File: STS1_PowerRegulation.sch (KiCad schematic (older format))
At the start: 16 parts, among them U2 TPS61288

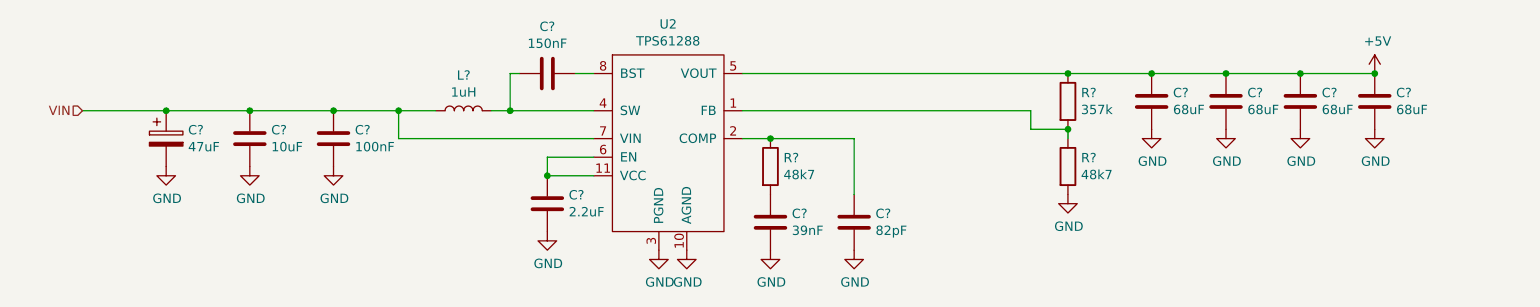
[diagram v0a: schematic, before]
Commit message: Select parts for dcdc converter
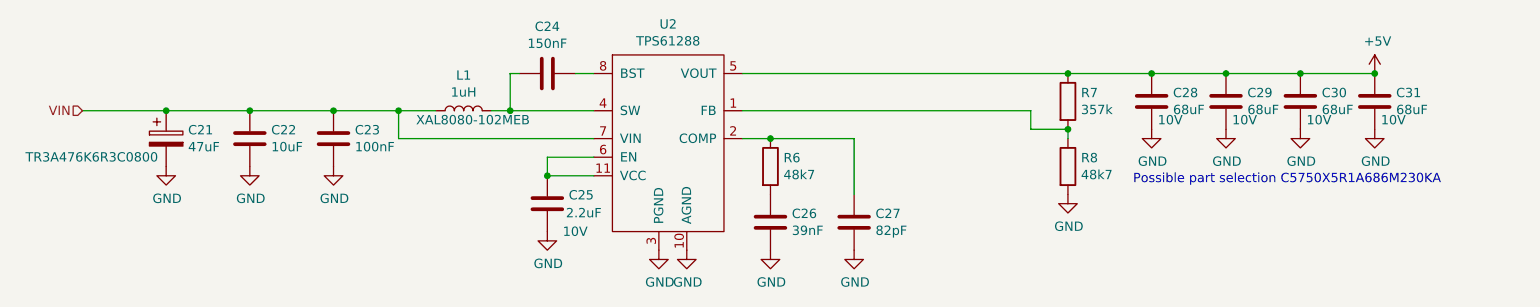
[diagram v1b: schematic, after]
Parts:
- C21: renamed from C?; footprint (none) -> Capacitor_Tantalum_SMD:CP_EIA-3216-18_Kemet-A; Part (none) -> TR3A476K6R3C0800
- C22: renamed from C?; footprint (none) -> Capacitor_SMD:C_1206_3216Metric
- C23, C24, C26, C27: renamed from C?; footprint (none) -> Capacitor_SMD:C_0603_1608Metric
- C25: renamed from C?; footprint (none) -> Capacitor_SMD:C_0603_1608Metric; Part (none) -> C1608X7R1A225K080AC; Voltage (none) -> 10V
- C28, C29, C30, C31: renamed from C?; footprint (none) -> Capacitor_SMD:C_2220_5650Metric; Part (none) -> C5750X5R1A686M230KA; Voltage (none) -> 10V
- L1: renamed from L?; footprint (none) -> STS1_DCDC:XAL8080; Part (none) -> XAL8080-102MEB
- R6, R7, R8: renamed from R?; footprint (none) -> Resistor_SMD:R_0603_1608Metric
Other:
- note added: "Possible part selection C5750X5R1A686M230KA"
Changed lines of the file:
@@
 $EndComp
 $Comp
-L Device:C C?
+L Device:C C25
 U 1 1 61712450
 P 4550 3300
-F 0 "C?" H 4665 3346 50  0000 L CNN
-F 1 "2.2uF" H 4665 3255 50  0000 L CNN
-F 2 "" H 4588 3150 50  0001 C CNN
+F 0 "C25" H 4665 3346 50  0000 L CNN
+F 1 "2.2uF" H 4650 3250 50  0000 L CNN
+F 2 "Capacitor_SMD:C_0603_1608Metric" H 4588 3150 50  0001 C CNN
 F 3 "~" H 4550 3300 50  0001 C CNN
+F 4 "10V" H 4700 3150 50  0000 C CNN "Voltage"
+F 5 "C1608X7R1A225K080AC " H 4550 3300 50  0001 C CNN "Part"
 	1    4550 3300
 	1    0    0    -1
 $EndComp
 $Comp
-L power:GND #PWR?
+L power:GND #PWR04
 U 1 1 61712809
 P 4550 3450
-F 0 "#PWR?" H 4550 3200 50  0001 C CNN
+F 0 "#PWR04" H 4550 3200 50  0001 C CNN
 F 1 "GND" H 4555 3277 50  0000 C CNN
 F 2 "" H 4550 3450 50  0001 C CNN
@@
 Connection ~ 4550 3150
 $Comp
-L Device:L L?
+L Device:L L1
 U 1 1 61712D19
 P 4100 2800
-F 0 "L?" V 4290 2800 50  0000 C CNN
+F 0 "L1" V 4290 2800 50  0000 C CNN
 F 1 "1uH" V 4199 2800 50  0000 C CNN
-F 2 "" H 4100 2800 50  0001 C CNN
+F 2 "STS1_DCDC:XAL8080" H 4100 2800 50  0001 C CNN
 F 3 "~" H 4100 2800 50  0001 C CNN
+F 4 "XAL8080-102MEB " V 4050 2750 50  0000 C CNN "Part"
 	1    4100 2800
 	0    -1   -1   0
@@
 	4250 2800 4350 2800
 $Comp
-L Device:C C?
+L Device:C C24
 U 1 1 617133FA
 P 4550 2600
-F 0 "C?" V 4298 2600 50  0000 C CNN
+F 0 "C24" V 4298 2600 50  0000 C CNN
 F 1 "150nF" V 4389 2600 50  0000 C CNN
-F 2 "" H 4588 2450 50  0001 C CNN
+F 2 "Capacitor_SMD:C_0603_1608Metric" H 4588 2450 50  0001 C CNN
 F 3 "~" H 4550 2600 50  0001 C CNN
 	1    4550 2600
@@
 	3750 2800 3950 2800
 $Comp
-L Device:C C?
+L Device:C C23
 U 1 1 61713BDE
 P 3400 2950
-F 0 "C?" H 3515 2996 50  0000 L CNN
+F 0 "C23" H 3515 2996 50  0000 L CNN
 F 1 "100nF" H 3515 2905 50  0000 L CNN
-F 2 "" H 3438 2800 50  0001 C CNN
+F 2 "Capacitor_SMD:C_0603_1608Metric" H 3438 2800 50  0001 C CNN
 F 3 "~" H 3400 2950 50  0001 C CNN
 	1    3400 2950
@@
 $EndComp
 $Comp
-L Device:C C?
+L Device:C C22
 U 1 1 61714238
 P 2950 2950
-F 0 "C?" H 3065 2996 50  0000 L CNN
+F 0 "C22" H 3065 2996 50  0000 L CNN
 F 1 "10uF" H 3065 2905 50  0000 L CNN
-F 2 "" H 2988 2800 50  0001 C CNN
+F 2 "Capacitor_SMD:C_1206_3216Metric" H 2988 2800 50  0001 C CNN
 F 3 "~" H 2950 2950 50  0001 C CNN
 	1    2950 2950
@@
 $EndComp
 $Comp
-L Device:CP C?
+L Device:CP C21
 U 1 1 61714747
 P 2500 2950
-F 0 "C?" H 2618 2996 50  0000 L CNN
+F 0 "C21" H 2618 2996 50  0000 L CNN
 F 1 "47uF" H 2618 2905 50  0000 L CNN
-F 2 "" H 2538 2800 50  0001 C CNN
+F 2 "Capacitor_Tantalum_SMD:CP_EIA-3216-18_Kemet-A" H 2538 2800 50  0001 C CNN
 F 3 "~" H 2500 2950 50  0001 C CNN
+F 4 "TR3A476K6R3C0800 " H 2100 2850 50  0000 C CNN "Part"
 	1    2500 2950
 	1    0    0    -1
 $EndComp
 $Comp
-L power:GND #PWR?
+L power:GND #PWR03
 U 1 1 61714EC5
 P 3400 3100
-F 0 "#PWR?" H 3400 2850 50  0001 C CNN
+F 0 "#PWR03" H 3400 2850 50  0001 C CNN
 F 1 "GND" H 3405 2927 50  0000 C CNN
 F 2 "" H 3400 3100 50  0001 C CNN
@@
 $EndComp
 $Comp
-L power:GND #PWR?
+L power:GND #PWR02
 U 1 1 617154C8
 P 2950 3100
-F 0 "#PWR?" H 2950 2850 50  0001 C CNN
+F 0 "#PWR02" H 2950 2850 50  0001 C CNN
 F 1 "GND" H 2955 2927 50  0000 C CNN
 F 2 "" H 2950 3100 50  0001 C CNN
@@
 $EndComp
 $Comp
-L power:GND #PWR?
+L power:GND #PWR01
 U 1 1 617158AD
 P 2500 3100
-F 0 "#PWR?" H 2500 2850 50  0001 C CNN
+F 0 "#PWR01" H 2500 2850 50  0001 C CNN
 F 1 "GND" H 2505 2927 50  0000 C CNN
 F 2 "" H 2500 3100 50  0001 C CNN
@@
 VIN
 $Comp
-L power:GND #PWR?
+L power:GND #PWR05
 U 1 1 617163D0
 P 5150 3550
-F 0 "#PWR?" H 5150 3300 50  0001 C CNN
+F 0 "#PWR05" H 5150 3300 50  0001 C CNN
 F 1 "GND" H 5155 3377 50  0000 C CNN
 F 2 "" H 5150 3550 50  0001 C CNN
@@
 $EndComp
 $Comp
-L power:GND #PWR?
+L power:GND #PWR06
 U 1 1 617168F0
 P 5300 3550
-F 0 "#PWR?" H 5300 3300 50  0001 C CNN
+F 0 "#PWR06" H 5300 3300 50  0001 C CNN
 F 1 "GND" H 5305 3377 50  0000 C CNN
 F 2 "" H 5300 3550 50  0001 C CNN
@@
 	5600 2600 7350 2600
 $Comp
-L Device:R R?
+L Device:R R7
 U 1 1 61717075
 P 7350 2750
-F 0 "R?" H 7420 2796 50  0000 L CNN
+F 0 "R7" H 7420 2796 50  0000 L CNN
 F 1 "357k" H 7420 2705 50  0000 L CNN
-F 2 "" V 7280 2750 50  0001 C CNN
+F 2 "Resistor_SMD:R_0603_1608Metric" V 7280 2750 50  0001 C CNN
 F 3 "~" H 7350 2750 50  0001 C CNN
 	1    7350 2750
@@
 $EndComp
 $Comp
-L Device:R R?
+L Device:R R8
 U 1 1 61717628
 P 7350 3100
-F 0 "R?" H 7420 3146 50  0000 L CNN
+F 0 "R8" H 7420 3146 50  0000 L CNN
 F 1 "48k7" H 7420 3055 50  0000 L CNN
-F 2 "" V 7280 3100 50  0001 C CNN
+F 2 "Resistor_SMD:R_0603_1608Metric" V 7280 3100 50  0001 C CNN
 F 3 "~" H 7350 3100 50  0001 C CNN
 	1    7350 3100
@@
 $EndComp
 $Comp
-L power:GND #PWR?
+L power:GND #PWR09
 U 1 1 61717E4B
 P 7350 3250
-F 0 "#PWR?" H 7350 3000 50  0001 C CNN
+F 0 "#PWR09" H 7350 3000 50  0001 C CNN
 F 1 "GND" H 7355 3077 50  0000 C CNN
 F 2 "" H 7350 3250 50  0001 C CNN
@@
 Connection ~ 7350 2900
 $Comp
-L Device:R R?
+L Device:R R6
 U 1 1 61718B8B
 P 5750 3100
-F 0 "R?" H 5820 3146 50  0000 L CNN
+F 0 "R6" H 5820 3146 50  0000 L CNN
 F 1 "48k7" H 5820 3055 50  0000 L CNN
-F 2 "" V 5680 3100 50  0001 C CNN
+F 2 "Resistor_SMD:R_0603_1608Metric" V 5680 3100 50  0001 C CNN
 F 3 "~" H 5750 3100 50  0001 C CNN
 	1    5750 3100
@@
 $EndComp
 $Comp
-L Device:C C?
+L Device:C C26
 U 1 1 617191CB
 P 5750 3400
-F 0 "C?" H 5865 3446 50  0000 L CNN
+F 0 "C26" H 5865 3446 50  0000 L CNN
 F 1 "39nF" H 5865 3355 50  0000 L CNN
-F 2 "" H 5788 3250 50  0001 C CNN
+F 2 "Capacitor_SMD:C_0603_1608Metric" H 5788 3250 50  0001 C CNN
 F 3 "~" H 5750 3400 50  0001 C CNN
 	1    5750 3400
@@
 $EndComp
 $Comp
-L power:GND #PWR?
+L power:GND #PWR07
 U 1 1 617197CA
 P 5750 3550
-F 0 "#PWR?" H 5750 3300 50  0001 C CNN
+F 0 "#PWR07" H 5750 3300 50  0001 C CNN
 F 1 "GND" H 5755 3377 50  0000 C CNN
 F 2 "" H 5750 3550 50  0001 C CNN
@@
 	5600 2950 5750 2950
 $Comp
-L Device:C C?
+L Device:C C27
 U 1 1 61719FDA
 P 6200 3400
-F 0 "C?" H 6315 3446 50  0000 L CNN
+F 0 "C27" H 6315 3446 50  0000 L CNN
 F 1 "82pF" H 6315 3355 50  0000 L CNN
-F 2 "" H 6238 3250 50  0001 C CNN
+F 2 "Capacitor_SMD:C_0603_1608Metric" H 6238 3250 50  0001 C CNN
 F 3 "~" H 6200 3400 50  0001 C CNN
 	1    6200 3400
@@
 $EndComp
 $Comp
-L power:GND #PWR?
+L power:GND #PWR08
 U 1 1 6171A582
 P 6200 3550
-F 0 "#PWR?" H 6200 3300 50  0001 C CNN
+F 0 "#PWR08" H 6200 3300 50  0001 C CNN
 F 1 "GND" H 6205 3377 50  0000 C CNN
 F 2 "" H 6200 3550 50  0001 C CNN
@@
 Connection ~ 5750 2950
 $Comp
-L Device:C C?
+L Device:C C28
 U 1 1 6171AF96
 P 7800 2750
-F 0 "C?" H 7915 2796 50  0000 L CNN
+F 0 "C28" H 7915 2796 50  0000 L CNN
 F 1 "68uF" H 7915 2705 50  0000 L CNN
-F 2 "" H 7838 2600 50  0001 C CNN
+F 2 "Capacitor_SMD:C_2220_5650Metric" H 7838 2600 50  0001 C CNN
 F 3 "~" H 7800 2750 50  0001 C CNN
+F 4 "10V" H 7900 2650 50  0000 C CNN "Voltage"
+F 5 "C5750X5R1A686M230KA " H 7800 2750 50  0001 C CNN "Part"
 	1    7800 2750
 	1    0    0    -1
 $EndComp
 $Comp
-L Device:C C?
+L Device:C C29
 U 1 1 6171B43B
 P 8200 2750
-F 0 "C?" H 8315 2796 50  0000 L CNN
+F 0 "C29" H 8315 2796 50  0000 L CNN
 F 1 "68uF" H 8315 2705 50  0000 L CNN
-F 2 "" H 8238 2600 50  0001 C CNN
+F 2 "Capacitor_SMD:C_2220_5650Metric" H 8238 2600 50  0001 C CNN
 F 3 "~" H 8200 2750 50  0001 C CNN
+F 4 "10V" H 8300 2650 50  0000 C CNN "Voltage"
+F 5 "C5750X5R1A686M230KA " H 8200 2750 50  0001 C CNN "Part"
 	1    8200 2750
 	1    0    0    -1
 $EndComp
 $Comp
-L Device:C C?
+L Device:C C30
 U 1 1 6171B9A7
 P 8600 2750
-F 0 "C?" H 8715 2796 50  0000 L CNN
+F 0 "C30" H 8715 2796 50  0000 L CNN
 F 1 "68uF" H 8715 2705 50  0000 L CNN
-F 2 "" H 8638 2600 50  0001 C CNN
+F 2 "Capacitor_SMD:C_2220_5650Metric" H 8638 2600 50  0001 C CNN
 F 3 "~" H 8600 2750 50  0001 C CNN
+F 4 "10V" H 8700 2650 50  0000 C CNN "Voltage"
+F 5 "C5750X5R1A686M230KA " H 8600 2750 50  0001 C CNN "Part"
 	1    8600 2750
 	1    0    0    -1
 $EndComp
 $Comp
-L Device:C C?
+L Device:C C31
 U 1 1 6171BF8D
 P 9000 2750
-F 0 "C?" H 9115 2796 50  0000 L CNN
+F 0 "C31" H 9115 2796 50  0000 L CNN
 F 1 "68uF" H 9115 2705 50  0000 L CNN
-F 2 "" H 9038 2600 50  0001 C CNN
+F 2 "Capacitor_SMD:C_2220_5650Metric" H 9038 2600 50  0001 C CNN
 F 3 "~" H 9000 2750 50  0001 C CNN
+F 4 "10V" H 9100 2650 50  0000 C CNN "Voltage"
+F 5 "C5750X5R1A686M230KA " H 9000 2750 50  0001 C CNN "Part"
 	1    9000 2750
 	1    0    0    -1
 $EndComp
 $Comp
-L power:GND #PWR?
+L power:GND #PWR010
 U 1 1 6171D90A
 P 7800 2900
-F 0 "#PWR?" H 7800 2650 50  0001 C CNN
+F 0 "#PWR010" H 7800 2650 50  0001 C CNN
 F 1 "GND" H 7805 2727 50  0000 C CNN
 F 2 "" H 7800 2900 50  0001 C CNN
@@
 $EndComp
 $Comp
-L power:GND #PWR?
+L power:GND #PWR011
 U 1 1 6171E089
 P 8200 2900
-F 0 "#PWR?" H 8200 2650 50  0001 C CNN
+F 0 "#PWR011" H 8200 2650 50  0001 C CNN
 F 1 "GND" H 8205 2727 50  0000 C CNN
 F 2 "" H 8200 2900 50  0001 C CNN
@@
 $EndComp
 $Comp
-L power:GND #PWR?
+L power:GND #PWR012
 U 1 1 6171E793
 P 8600 2900
-F 0 "#PWR?" H 8600 2650 50  0001 C CNN
+F 0 "#PWR012" H 8600 2650 50  0001 C CNN
 F 1 "GND" H 8605 2727 50  0000 C CNN
 F 2 "" H 8600 2900 50  0001 C CNN
@@
 $EndComp
 $Comp
-L power:GND #PWR?
+L power:GND #PWR014
 U 1 1 6171EEB6
 P 9000 2900
-F 0 "#PWR?" H 9000 2650 50  0001 C CNN
+F 0 "#PWR014" H 9000 2650 50  0001 C CNN
 F 1 "GND" H 9005 2727 50  0000 C CNN
 F 2 "" H 9000 2900 50  0001 C CNN
@@
 	8600 2600 9000 2600
 $Comp
-L power:+5V #PWR?
+L power:+5V #PWR013
 U 1 1 6171F991
 P 9000 2600
-F 0 "#PWR?" H 9000 2450 50  0001 C CNN
+F 0 "#PWR013" H 9000 2450 50  0001 C CNN
 F 1 "+5V" H 9015 2773 50  0000 C CNN
 F 2 "" H 9000 2600 50  0001 C CNN
@@
 $EndComp
 Connection ~ 9000 2600
+Text Notes 7700 3200 0    50   ~ 0
+Possible part selection C5750X5R1A686M230KA
 $EndSCHEMATC
